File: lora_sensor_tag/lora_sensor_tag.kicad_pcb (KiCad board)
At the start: 4 copper layers, 70 x 100 mm, 142 parts, among them J1 Conn_Coaxial, J2 Conn_Coaxial, J3 Li-ion_bat_conn, J4 USB_C_Receptacle_USB2.0_14P, Q1 NPN, Q2 NPN, Q3 NPN, SW1 SW_MCU_RST, SW2 SW_MCU_PROG, U1 SX1276IMLTRT, U2 ESP32-WROOM-32D, U3 PE4259, U4 SHT20, U5 TPS63070RNMR, U6 MCP73871-2CAI_ML, U7 AMS1117-3.3, U8 MAX17048G_T10, U9 CP2102N-Axx-xQFN28, Y1 32 MHz

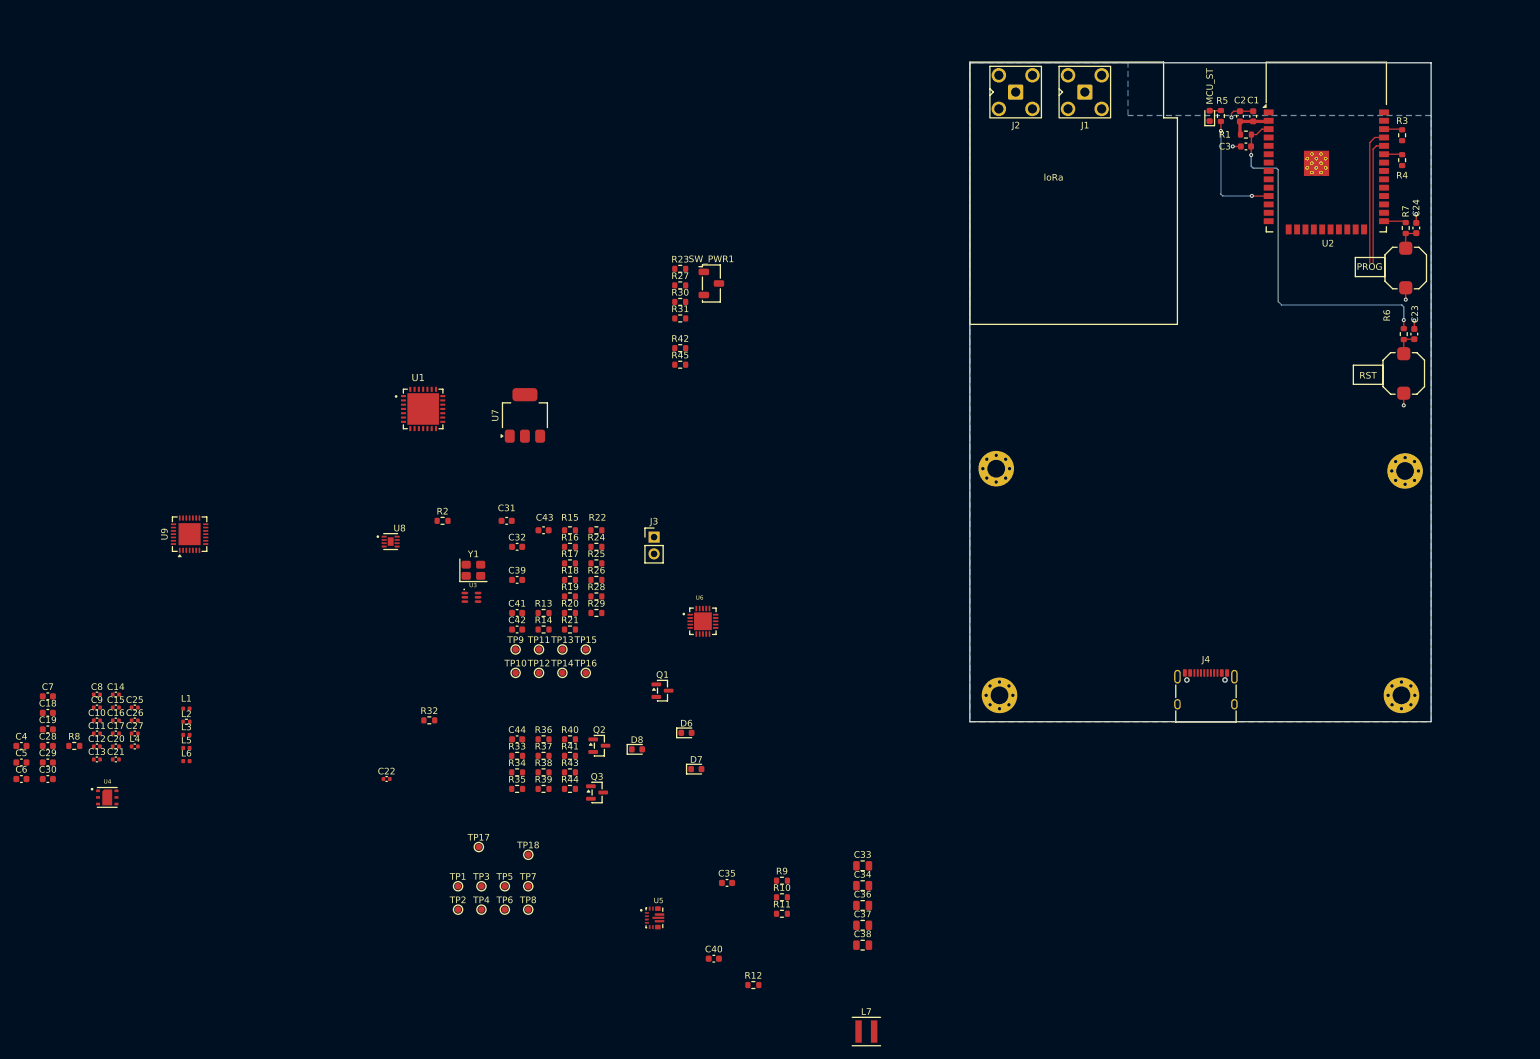
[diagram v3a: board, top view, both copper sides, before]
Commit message: Add USB and CP2102 initial layout
Signed-off-by: Volodymyr <volodymyrnoha99@gmail.com>
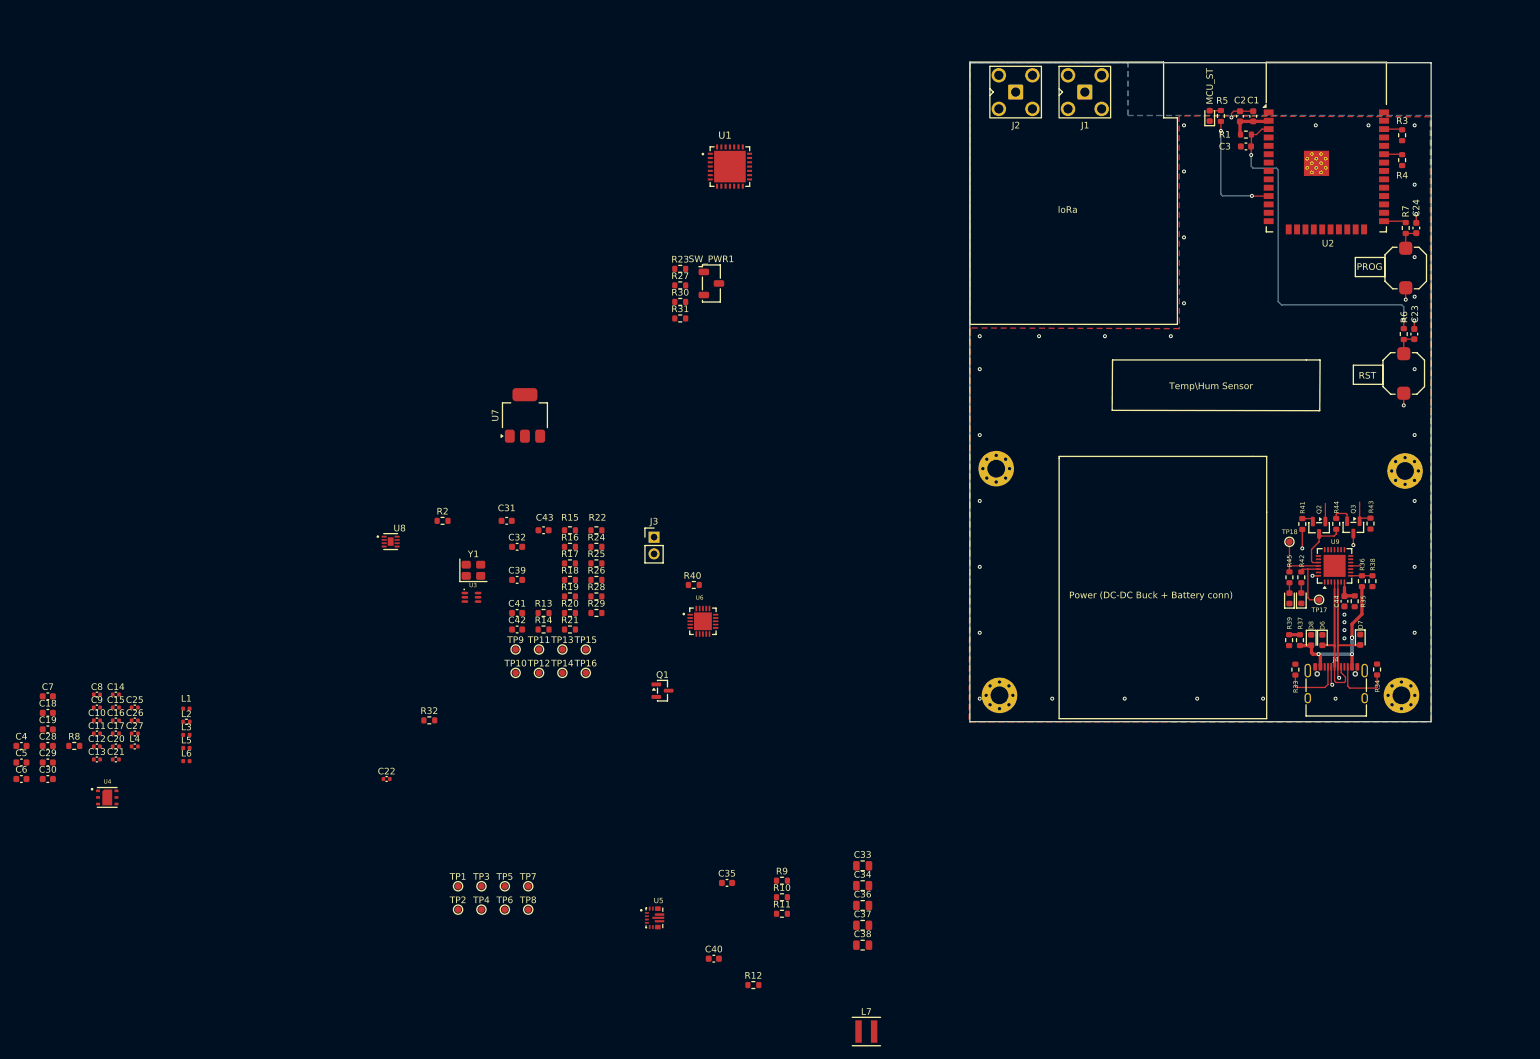
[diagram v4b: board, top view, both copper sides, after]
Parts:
- added D10: LED_TX, LED_SMD:LED_0603_1608Metric, F.Cu at (214.0, 114.8)
- added D9: LED_RX, LED_SMD:LED_0603_1608Metric, F.Cu at (215.8, 114.8)
- moved U9 173.8 mm to (220.8, 109.8)
- moved TP17 132.9 mm to (218.5, 115.0)
- moved R34 131.4 mm to (227.3, 125.6), turned to -90 degrees
- moved R35 130.3 mm to (223.9, 115.2), turned to -90 degrees
- moved R38 129.1 mm to (226.6, 112.2), turned to 90 degrees
- moved C44 127.3 mm to (222.3, 115.2), turned to -90 degrees
- moved R43 127.2 mm to (226.3, 103.4), turned to -90 degrees
- moved R36 126.5 mm to (225.0, 112.2), turned to -90 degrees
- moved TP18 124.9 mm to (214.0, 106.2)
- moved R44 123.0 mm to (221.1, 103.5), turned to 90 degrees
- moved Q3 121.6 mm to (223.7, 104.0), turned to -90 degrees
- moved R33 118.8 mm to (214.9, 125.6), turned to -90 degrees
- moved R41 116.6 mm to (215.9, 103.5), turned to 90 degrees
- moved R37 116.1 mm to (215.6, 121.1), turned to 90 degrees
- moved R39 115.4 mm to (213.9, 121.1), turned to -90 degrees
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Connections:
- net /usb_and_prog/USB_D_M renamed /usb_and_prog/USB_D_N
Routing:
- net VUSB: track 0.00 -> 23.9 mm, vias 0 -> 4
- net /usb_and_prog/USB_D_N: track 0.00 -> 23.8 mm, vias 0 -> 2
- net /usb_and_prog/USB_D_P: track 0.00 -> 22.0 mm
- net /usb_and_prog/DTR: track 0.00 -> 21.7 mm, vias 0 -> 3
- net /usb_and_prog/TX: track 20.8 -> 9.85 mm
- net /usb_and_prog/RX: track 19.2 -> 9.35 mm
- net Net-(J4-CC1): track 0.00 -> 9.59 mm
- net Net-(J4-CC2): track 0.00 -> 9.44 mm
- net /usb_and_prog/RTS: track 0.00 -> 9.34 mm
- net /MCU_main_part/MCU_IO0: track 3.39 -> 8.40 mm
- net 3V3: track 6.99 -> 10.6 mm
- net Net-(Q3-B): track 0.00 -> 3.40 mm
- net Net-(U9-VBUS): track 0.00 -> 3.30 mm
- net /MCU_main_part/MCU_EN: track 54.8 -> 57.6 mm
- net Net-(Q2-B): track 0.00 -> 2.05 mm
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- added copper zone on F.Cu, net GND
- added copper zone on In1.Cu, net GND
- added copper zone on In2.Cu, net GND
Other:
- board text added: "Power (DC-DC Buck + Battery conn)"
- board text added: "Temp\Hum Sensor"

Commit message: Update PCB layout routing
Updates and adds the following changes to the PCB
layout routing:
- Changed board dimensions and topology;
- Add layout for MCP73871 Li-ion battery charger;
- Add layout for MAX17048 Fuel Gauge;

Signed-off-by: Volodymyr <volodymyrnoha99@gmail.com>
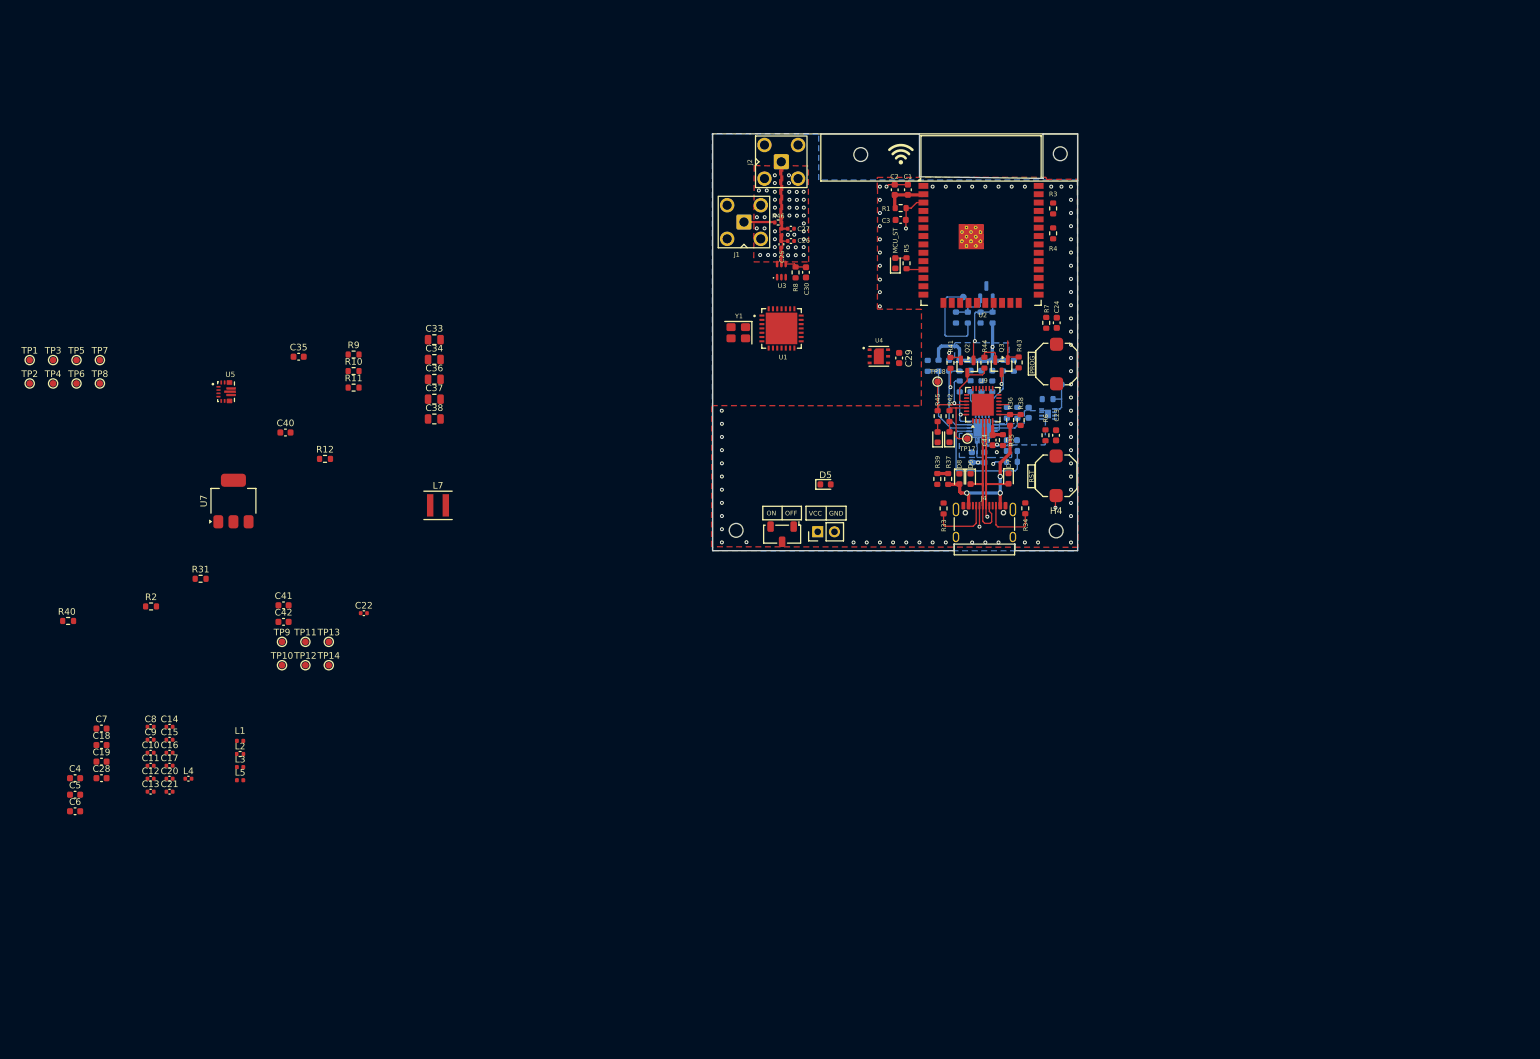
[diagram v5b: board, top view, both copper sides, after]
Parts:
- added D2: PG, LED_SMD:LED_0603_1608Metric, B.Cu at (165.6, 79.4)
- added D3: STAT2, LED_SMD:LED_0603_1608Metric, B.Cu at (167.2, 79.4)
- added D4: STAT1\LBO, LED_SMD:LED_0603_1608Metric, B.Cu at (168.9, 79.4)
- added D5: LED_PWR, LED_SMD:LED_0603_1608Metric, F.Cu at (143.6, 97.5)
- added G***: LOGO, wifi_sign:wifi_sign_footprint, F.Cu at (155.0, 47.2)
- added R46: 0R, Resistor_SMD:R_0402_1005Metric, F.Cu at (136.4, 57.7)
- C31, C32, C39, C43, Q1, R13, R14, R15, R16, R17, R18, R19, R20, R21, R22, R23, R24, R25, R26, R27, R28, R29, R30, R32, TP15, TP16, U6, U8: moved to B.Cu
- H1, H2, H3, H4: value MountingHole_Pad -> MountingHole; footprint MountingHole:MountingHole_2.7mm_M2.5_Pad_Via -> MountingHole:MountingHole_2.1mm
- moved C29 143.0 mm to (154.8, 78.3), turned to -90 degrees
- moved C30 138.4 mm to (140.6, 65.3), turned to 90 degrees
- moved U4 134.9 mm to (151.7, 78.0)
- moved R8 130.9 mm to (139.1, 65.3), turned to 90 degrees
- moved C27 125.6 mm to (138.3, 58.7), turned to 180 degrees
- moved C26 123.3 mm to (138.3, 60.5), turned to 180 degrees
- moved L6 120.8 mm to (136.9, 59.2), turned to 90 degrees
- moved C25 120.7 mm to (136.9, 61.0), turned to 90 degrees
- moved R32 105.7 mm to (177.3, 84.5), turned to 180 degrees
- moved C33 103.0 mm to (84.2, 75.5)
- moved C35 103.0 mm to (63.6, 78.1)
- moved C37 103.0 mm to (84.2, 84.5)
- moved R11 103.0 mm to (72.0, 82.8)
- moved R12 103.0 mm to (67.6, 93.6)
- moved TP6 103.0 mm to (29.9, 82.2)
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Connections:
- C27 pad 2: Net-(J1-In) -> Net-(J2-In)
- J2 pad 1: Net-(J1-In) -> Net-(J2-In)
- L6 pad 2: Net-(J1-In) -> Net-(J2-In)
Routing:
- net /MCU_main_part/MCU_EN: track 57.6 -> 8.85 mm, vias 2 -> 1
- net VUSB: track 23.9 -> 61.3 mm, vias 4 -> 5
- net /power/CE: track 0.00 -> 28.8 mm, vias 0 -> 2
- net /power/VPCC: track 0.00 -> 20.0 mm
- net /MCU_main_part/MCU_ST: track 18.4 -> 2.61 mm, vias 2 -> 0
- net Net-(U6-SEL): track 0.00 -> 13.9 mm
- net /MCU_main_part/GPIO_CE: track 0.00 -> 13.8 mm
- net Net-(U6-PROG2): track 0.00 -> 12.2 mm
- net Net-(J2-In): track 0.00 -> 11.2 mm
- net Net-(U6-~{TE}): track 0.00 -> 9.44 mm
- net /MCU_main_part/GPIO_PG_ALERT: track 0.00 -> 5.92 mm, vias 0 -> 2
- net Net-(U6-THERM): track 0.00 -> 5.84 mm
- net Net-(Q1-B): track 0.00 -> 5.65 mm
- net Net-(J1-In): track 0.00 -> 4.72 mm
- net Net-(U6-PROG1): track 0.00 -> 4.67 mm
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- added copper zone on B.Cu, net VBAT
- added copper zone on B.Cu, net VOUT
- added copper zone on B.Cu, net VUSB
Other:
- board size 70 x 100 mm -> 55.4 x 63.3 mm
- board text added: "Charger + Fuel Gauge (bottom layer)"
- board text added: "GND"
- board text added: "LoRa Temp\Hum Sensor V1.0"
- board text added: "OFF"
- board text added: "ON"
- board text added: "VCC"
- board text removed: "loRa"

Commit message: Comment and capasitor formfactor.
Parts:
- removed C42: 22uF, Capacitor_SMD:C_0603_1608Metric
- removed TP13: TestPoint, TestPoint:TestPoint_Pad_D1.0mm
- removed U7: AMS1117-3.3, Package_TO_SOT_SMD:SOT-223-3_TabPin2
- C40: footprint Capacitor_SMD:C_0603_1608Metric -> Capacitor_SMD:C_0402_1005Metric
- R10: value 680K -> 470K
- R12: value 130K -> 150K
- R9: value R -> 100K
- moved C41 30.8 mm to (83.0, 94.0)
- moved U5 24.7 mm to (76.0, 91.5)
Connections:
- C36 pad 1: V5 -> 3V3
- C37 pad 1: V5 -> 3V3
- C38 pad 1: V5 -> 3V3
- C41 pad 1: V5 -> 3V3
- R10 pad 1: V5 -> 3V3
- R9 pad 2: V5 -> 3V3
- U5 pad 7_8: V5 -> 3V3
